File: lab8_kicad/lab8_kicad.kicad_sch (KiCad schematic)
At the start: 24 parts, among them M1 Motor, SW1 Reset, U1 SN754410, U2 PIC32MX170F256B, U4 Quadrature_Encoder

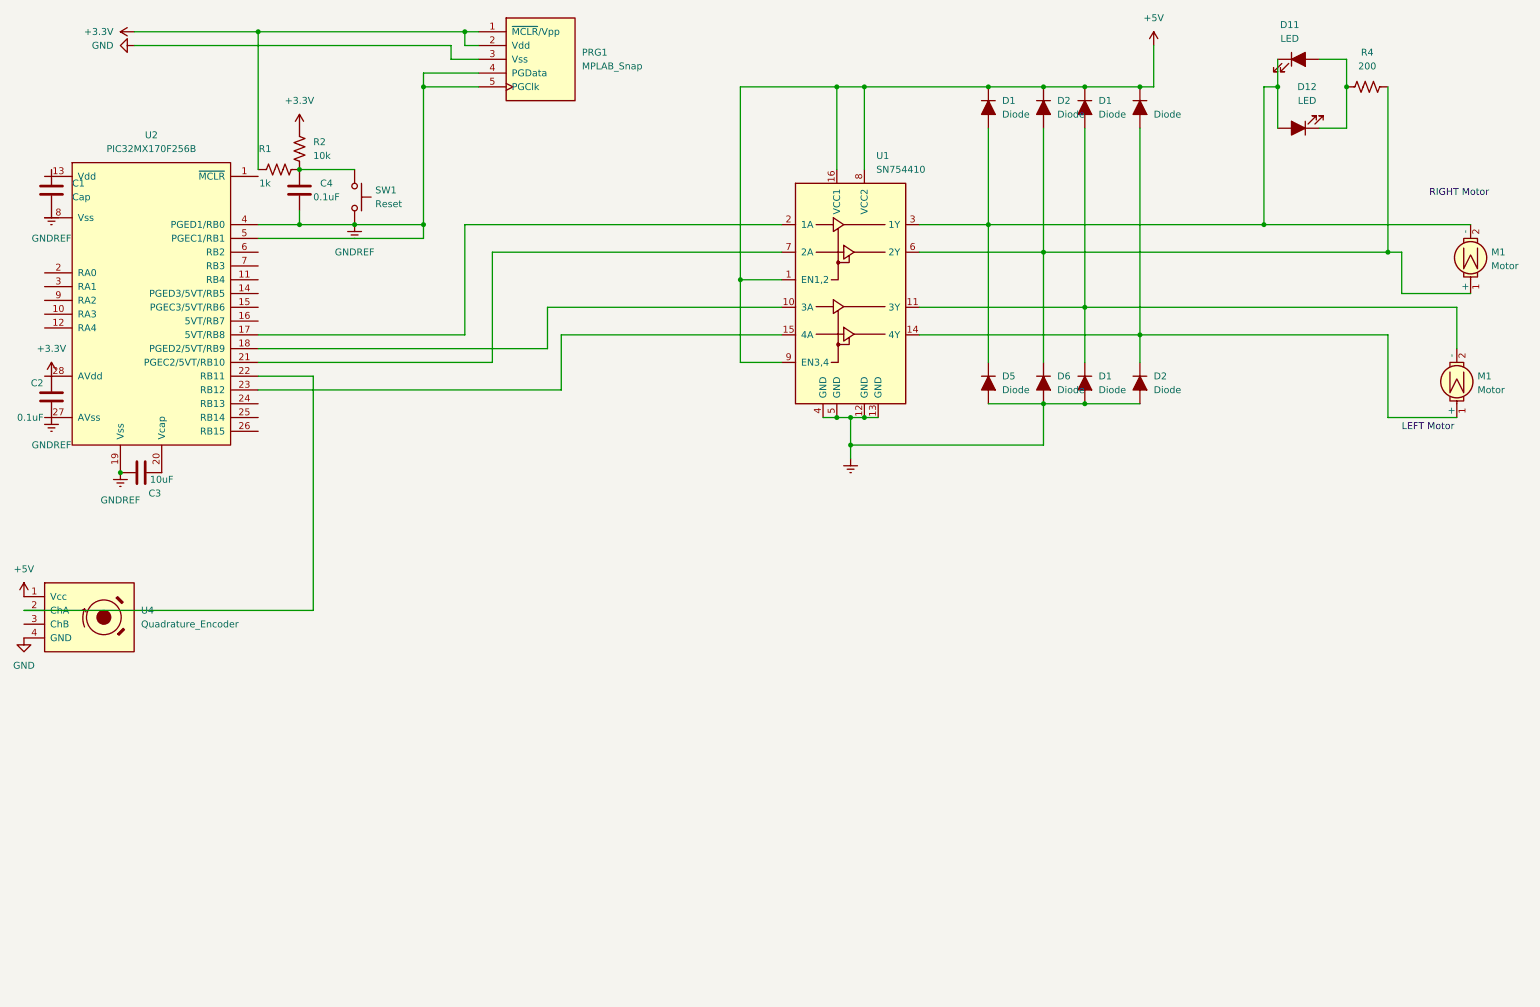
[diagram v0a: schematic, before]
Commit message: Updated Circuit Schematic (Include Cmd Gen)
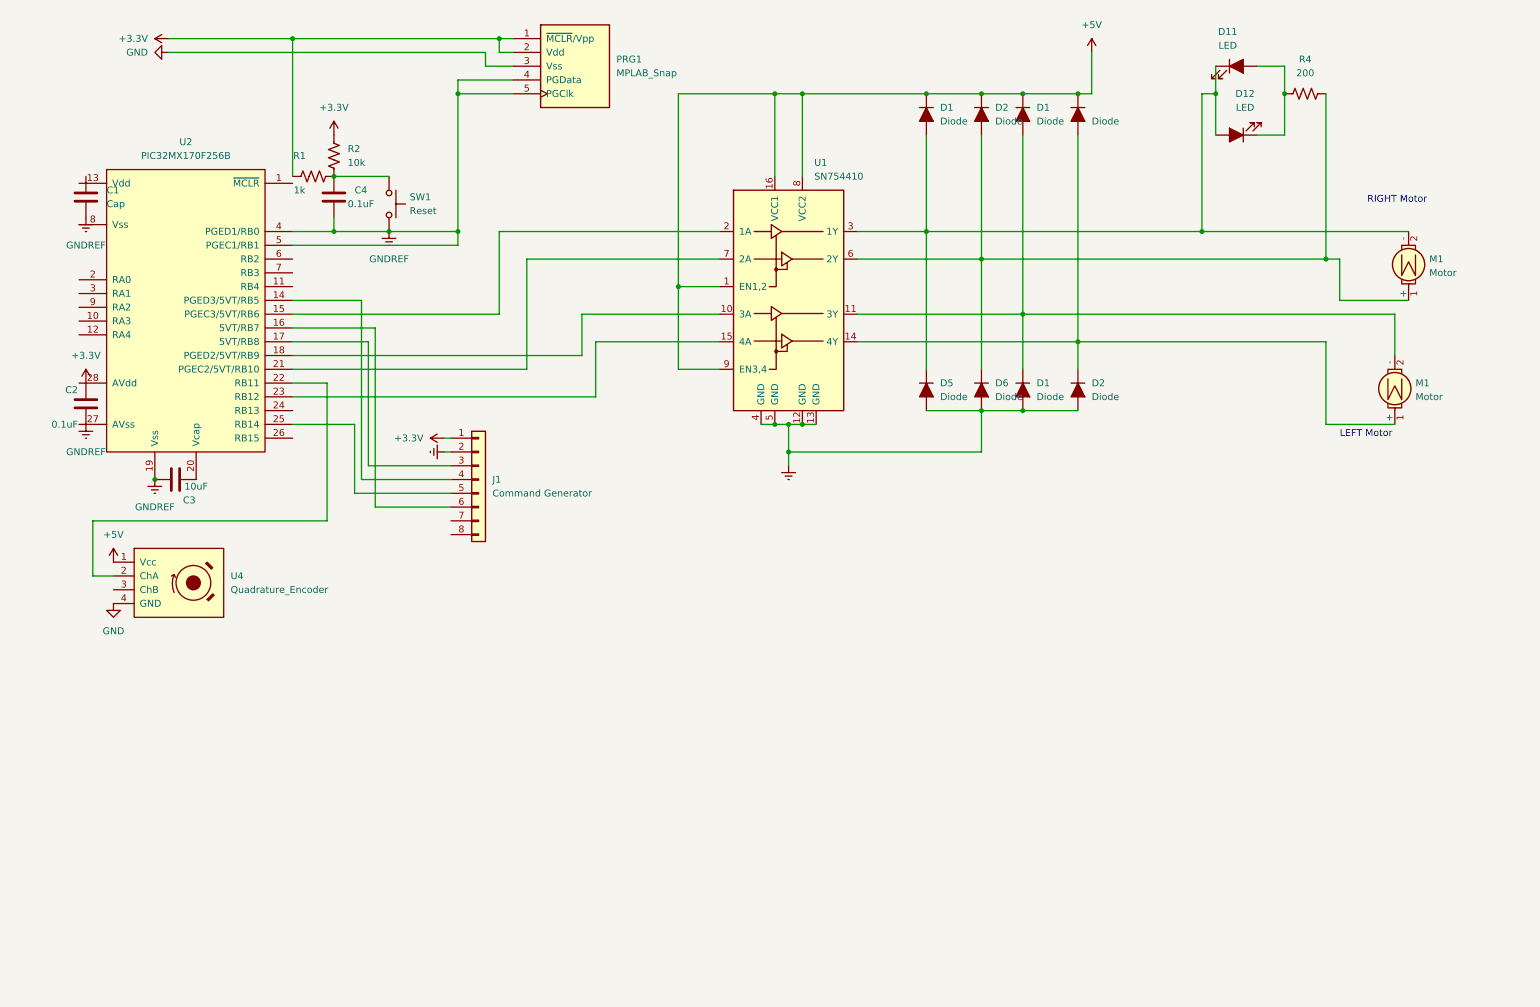
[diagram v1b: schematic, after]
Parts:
- added J1: Command Generator, symbol ME218_BaseLib:Molex8
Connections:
- net +3.3V: now also J1.1 (Pin_1)
- net Earth: now also J1.2 (Pin_2)
- net at U2.17 (5VT/RB8): now also J1.3 (Pin_3); no longer U1.2 (1A)
- net at U2.14 (PGED3/5VT/RB5): now also J1.4 (Pin_4)
- net at U2.15 (PGEC3/5VT/RB6): now also U1.2 (1A)
- net at U2.16 (5VT/RB7): now also J1.6 (Pin_6)
- net at U2.25 (RB14): now also J1.5 (Pin_5)
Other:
- moved on the sheet: C1, C2, C3, C4, D1, D11, D12, D2, D5, D6, M1, PRG1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

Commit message: fix schematic
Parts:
- removed U4: Quadrature_Encoder, symbol ME218_BaseLib:Quadrature_Encoder
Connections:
- net +3.3V: no longer PRG1.1 (~{MCLR}/Vpp), R1.1
- net GNDREF: no longer PRG1.4 (PGData), PRG1.5 (PGClk), U2.4 (PGED1/RB0), U2.5 (PGEC1/RB1)
- net at J1.6 (Pin_6): now also U2.11 (RB4); no longer U2.16 (5VT/RB7)
- net at U2.1 (~{MCLR}): now also PRG1.1 (~{MCLR}/Vpp), R1.1
- new net: PRG1.4 (PGData), U2.4 (PGED1/RB0)
- new net: PRG1.5 (PGClk), U2.5 (PGEC1/RB1)
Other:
- moved on the sheet: C1, C2, C3, C4, D1, D11, D12, D2, D5, D6, J1, M1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

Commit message: suibian
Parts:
- added J2: Reflective Opto-sensor, symbol ME218_BaseLib:Molex4
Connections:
- net +3.3V: now also J2.1 (Pin_1)
- net GND: now also J2.2 (Pin_2)
- net BI-CONSENSOR: now reaches U2.23 (RB12)
- net BI-CONSENSOR: no longer U1.15 (4A)
- net at U1.2 (1A): now also U2.6 (RB2); no longer U2.15 (PGEC3/5VT/RB6)
- net OC1: now reaches U1.7 (2A)
- net OC1: now also U2.7 (RB3); no longer U2.21 (PGEC2/5VT/RB10)
- net tera: now reaches U2.16 (5VT/RB7)
- net tera: now also U2.15 (PGEC3/5VT/RB6)
- net tape sensor: now reaches U2.9 (RA2)
- net tape sensor: now also J2.3 (Pin_3)
- new net OC3: U1.15 (4A), U2.21 (PGEC2/5VT/RB10)
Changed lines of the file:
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@@
+    (stroke (width 0) (type default))
+  )
+  (wire (pts (xy 104.14 60.96) (xy 66.04 60.96))
+    (stroke (width 0) (type default))
+  )
+  (wire (pts (xy 104.14 55.88) (xy 104.14 60.96))
     (stroke (width 0) (type default))
   )
@@
     (stroke (width 0) (type default))
   )
-  (wire (pts (xy 104.14 55.88) (xy 104.14 71.12))
-    (stroke (width 0) (type default))
-  )
   (wire (pts (xy 210.82 38.1) (xy 210.82 76.2))
     (stroke (width 0) (type default))
@@
     (stroke (width 0) (type default))
   )
+  (wire (pts (xy 109.22 63.5) (xy 66.04 63.5))
+    (stroke (width 0) (type default))
+  )
   (wire (pts (xy 256.54 91.44) (xy 269.24 91.44))
     (stroke (width 0) (type default))
   )
-  (wire (pts (xy 109.22 60.96) (xy 109.22 81.28))
-    (stroke (width 0) (type default))
-  )
   (wire (pts (xy 259.08 68.58) (xy 271.78 68.58))
     (stroke (width 0) (type default))
   )
-  (wire (pts (xy 66.04 71.12) (xy 104.14 71.12))
-    (stroke (width 0) (type default))
-  )
   (wire (pts (xy 73.66 38.1) (xy 83.82 38.1))
     (stroke (width 0) (type default))
@@
     (stroke (width 0) (type default))
   )
-  (wire (pts (xy 121.92 86.36) (xy 121.92 76.2))
+  (wire (pts (xy 96.52 81.28) (xy 66.04 81.28))
+    (stroke (width 0) (type default))
+  )
+  (wire (pts (xy 20.32 128.27) (xy 20.32 69.85))
+    (stroke (width 0) (type default))
+  )
+  (wire (pts (xy 96.52 76.2) (xy 96.52 81.28))
     (stroke (width 0) (type default))
   )
@@
     (stroke (width 0) (type default))
   )
-  (wire (pts (xy 119.38 78.74) (xy 119.38 71.12))
-    (stroke (width 0) (type default))
-  )
-  (wire (pts (xy 121.92 76.2) (xy 144.78 76.2))
-    (stroke (width 0) (type default))
-  )
-  (wire (pts (xy 119.38 71.12) (xy 144.78 71.12))
+  (wire (pts (xy 91.44 78.74) (xy 66.04 78.74))
     (stroke (width 0) (type default))
   )
@@
     (stroke (width 0) (type default))
   )
+  (wire (pts (xy 20.32 69.85) (xy 26.67 69.85))
+    (stroke (width 0) (type default))
+  )
   (wire (pts (xy 144.78 66.04) (xy 137.16 66.04))
     (stroke (width 0) (type default))
@@
     (stroke (width 0) (type default))
   )
-  (wire (pts (xy 66.04 86.36) (xy 121.92 86.36))
+  (wire (pts (xy 106.68 128.27) (xy 20.32 128.27))
     (stroke (width 0) (type default))
   )
@@
     (stroke (width 0) (type default))
   )
+  (wire (pts (xy 144.78 76.2) (xy 96.52 76.2))
+    (stroke (width 0) (type default))
+  )
   (wire (pts (xy 243.84 25.4) (xy 248.92 25.4))
     (stroke (width 0) (type default))
@@
     (stroke (width 0) (type default))
   )
+  (wire (pts (xy 144.78 71.12) (xy 91.44 71.12))
+    (stroke (width 0) (type default))
+  )
   (wire (pts (xy 193.04 38.1) (xy 193.04 60.96))
     (stroke (width 0) (type default))
@@
     (stroke (width 0) (type default))
   )
-  (wire (pts (xy 66.04 81.28) (xy 109.22 81.28))
-    (stroke (width 0) (type default))
-  )
-  (wire (pts (xy 66.04 78.74) (xy 119.38 78.74))
+  (wire (pts (xy 91.44 71.12) (xy 91.44 78.74))
+    (stroke (width 0) (type default))
+  )
+  (wire (pts (xy 109.22 60.96) (xy 109.22 63.5))
     (stroke (width 0) (type default))
   )
@@
   (text "RIGHT Motor" (at 262.89 49.53 0)
     (effects (font (size 1.27 1.27)) (justify left bottom))
+  )
+  (global_label "tera" (shape input) (at 66.04 71.12 0) (fields_autoplaced)
+    (effects (font (size 1.27 1.27)) (justify left))
+    (property "Intersheetrefs" "${INTERSHEET_REFS}" (at 72.7747 71.12 0)
+      (effects (font (size 1.27 1.27)) (justify left) hide)
+    )
+  )
+  (global_label "OC3" (shape input) (at 102.87 76.2 0) (fields_autoplaced)
+    (effects (font (size 1.27 1.27)) (justify left))
+    (property "Intersheetrefs" "${INTERSHEET_REFS}" (at 109.6652 76.2 0)
+      (effects (font (size 1.27 1.27)) (justify left) hide)
+    )
+  )
+  (global_label "tape sensor" (shape input) (at 66.04 128.27 180) (fields_autoplaced)
+    (effects (font (size 1.27 1.27)) (justify right))
+    (property "Intersheetrefs" "${INTERSHEET_REFS}" (at 51.7459 128.27 0)
+      (effects (font (size 1.27 1.27)) (justify right) hide)
+    )
+  )
+  (global_label "BI-CONSENSOR" (shape input) (at 66.04 86.36 0) (fields_autoplaced)
+    (effects (font (size 1.27 1.27)) (justify left))
+    (property "Intersheetrefs" "${INTERSHEET_REFS}" (at 83.9024 86.36 0)
+      (effects (font (size 1.27 1.27)) (justify left) hide)
+    )
+  )
+  (global_label "tera" (shape input) (at 66.04 73.66 0) (fields_autoplaced)
+    (effects (font (size 1.27 1.27)) (justify left))
+    (property "Intersheetrefs" "${INTERSHEET_REFS}" (at 72.7747 73.66 0)
+      (effects (font (size 1.27 1.27)) (justify left) hide)
+    )
+  )
+  (global_label "OC1" (shape input) (at 101.6 63.5 0) (fields_autoplaced)
+    (effects (font (size 1.27 1.27)) (justify left))
+    (property "Intersheetrefs" "${INTERSHEET_REFS}" (at 108.3952 63.5 0)
+      (effects (font (size 1.27 1.27)) (justify left) hide)
+    )
   )
   (symbol (lib_id "ME218_BaseLib:SW_Push") (at 83.82 43.18 270) (unit 1)
@@
         (path "/c54286ed-3a82-4325-b913-88d6215d969b"
           (reference "D1") (unit 1)
+        )
+      )
+    )
+  )
+  (symbol (lib_id "power:+3.3V") (at 106.68 123.19 90) (unit 1)
+    (in_bom yes) (on_board yes) (dnp no) (fields_autoplaced)
+    (property "Reference" "#PWR09" (at 110.49 123.19 0)
+      (effects (font (size 1.27 1.27)) hide)
+    )
+    (property "Value" "+3.3V" (at 102.87 123.19 90)
+      (effects (font (size 1.27 1.27)) (justify left))
+    )
+    (property "Footprint" "" (at 106.68 123.19 0)
+      (effects (font (size 1.27 1.27)) hide)
+    )
+    (property "Datasheet" "" (at 106.68 123.19 0)
+      (effects (font (size 1.27 1.27)) hide)
+    )
+    (pin "1")
+    (instances
+      (project "lab8_kicad"
+        (path "/c3d935fb-33dd-45da-8182-93745821b586"
+          (reference "#PWR09") (unit 1)
         )
       )
@@
     )
   )
+  (symbol (lib_id "ME218_BaseLib:Molex4") (at 111.76 125.73 0) (unit 1)
+    (in_bom yes) (on_board yes) (dnp no) (fields_autoplaced)
+    (property "Reference" "J2" (at 114.3 125.73 0)
+      (effects (font (size 1.27 1.27)) (justify left))
+    )
+    (property "Value" "Reflective Opto-sensor" (at 114.3 128.27 0)
+      (effects (font (size 1.27 1.27)) (justify left))
+    )
+    (property "Footprint" "" (at 111.76 125.73 0)
+      (effects (font (size 1.27 1.27)) hide)
+    )
+    (property "Datasheet" "" (at 111.76 125.73 0)
+      (effects (font (size 1.27 1.27)) hide)
+    )
+    (pin "1")
+    (pin "2")
+    (pin "3")
+    (pin "4")
+    (instances
+      (project "lab8_kicad"
+        (path "/c3d935fb-33dd-45da-8182-93745821b586"
+          (reference "J2") (unit 1)
+        )
+      )
+    )
+  )
   (symbol (lib_id "ME218_BaseLib:LED") (at 240.03 25.4 0) (unit 1)
     (in_bom yes) (on_board yes) (dnp no) (fields_autoplaced)
@@
         )
       )
+    )
+  )
+  (symbol (lib_id "power:GND") (at 106.68 125.73 270) (unit 1)
+    (in_bom yes) (on_board yes) (dnp no) (fields_autoplaced)
+    (property "Reference" "#PWR010" (at 100.33 125.73 0)
+      (effects (font (size 1.27 1.27)) hide)
+    )
+    (property "Value" "GND" (at 102.87 125.73 90)
+      (effects (font (size 1.27 1.27)) (justify right))
+    )
+    (property "Footprint" "" (at 106.68 125.73 0)
+      (effects (font (size 1.27 1.27)) hide)
+    )
+    (property "Datasheet" "" (at 106.68 125.73 0)
+      (effects (font (size 1.27 1.27)) hide)
+    )
+    (pin "1")
+    (instances
+      (project "lab8_kicad"
+        (path "/c3d935fb-33dd-45da-8182-93745821b586"
+          (reference "#PWR010") (unit 1)
+        )
+      )

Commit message: fix schemetic
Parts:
- removed D11, D12: LED, symbol ME218_BaseLib:LED
- added Q1: Photo_NPN, symbol ME218_BaseLib:Photo_NPN
- added R5, R6: 10K, symbol ME218_BaseLib:Res1
- added U2: MCP6294, symbol ME218_BaseLib:MCP6294
- R4: value 200 -> 2K
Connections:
- net +5V: now also Q1.1 (C), R5.1, U2.4 (V+)
- net Earth: now also R6.2, U2.11 (V-)
- net at R4.1: now also Q1.2 (E), U2.2 (-)
- net at D2.2 (A), D6.1 (K), M1.1 (+)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: no longer R4.2
- net BI-CONSENSOR renamed BEACON_SENSOR
- net BEACON_SENSOR: now also R4.2, U2.1
- new net: R5.2, R6.1, U2.3 (+)

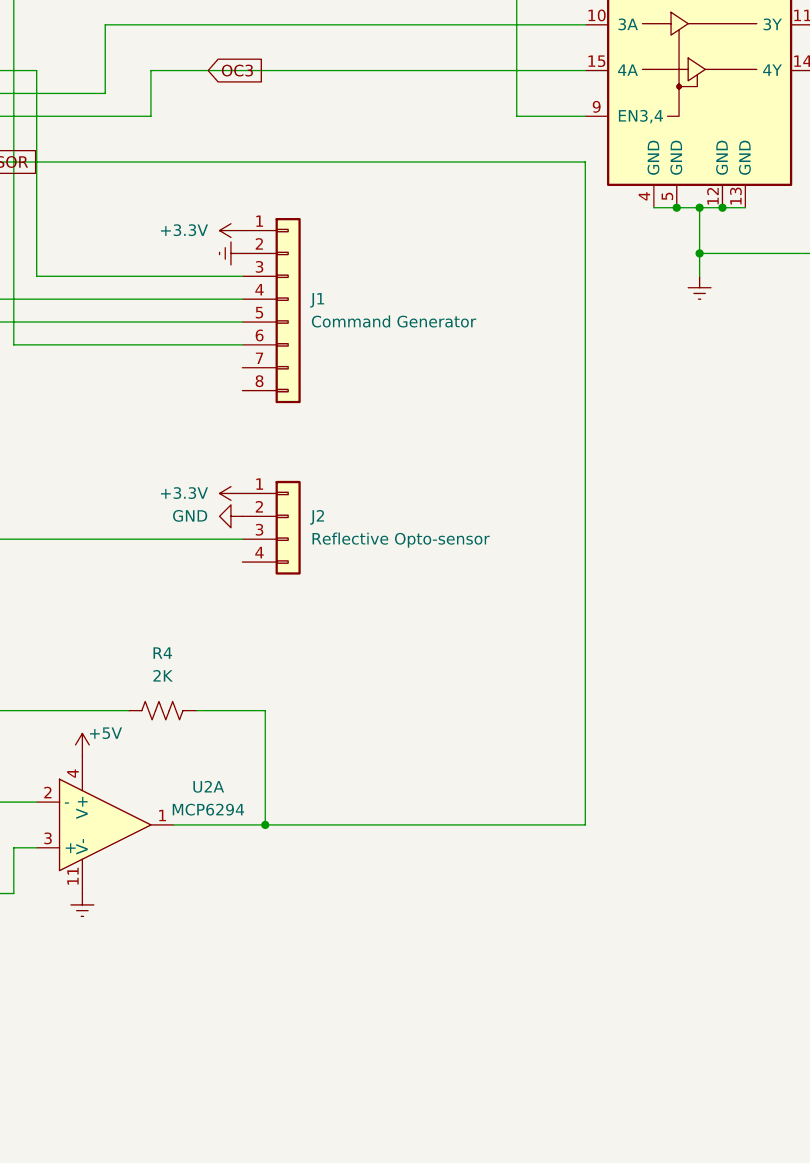
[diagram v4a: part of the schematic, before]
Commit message: add comparator
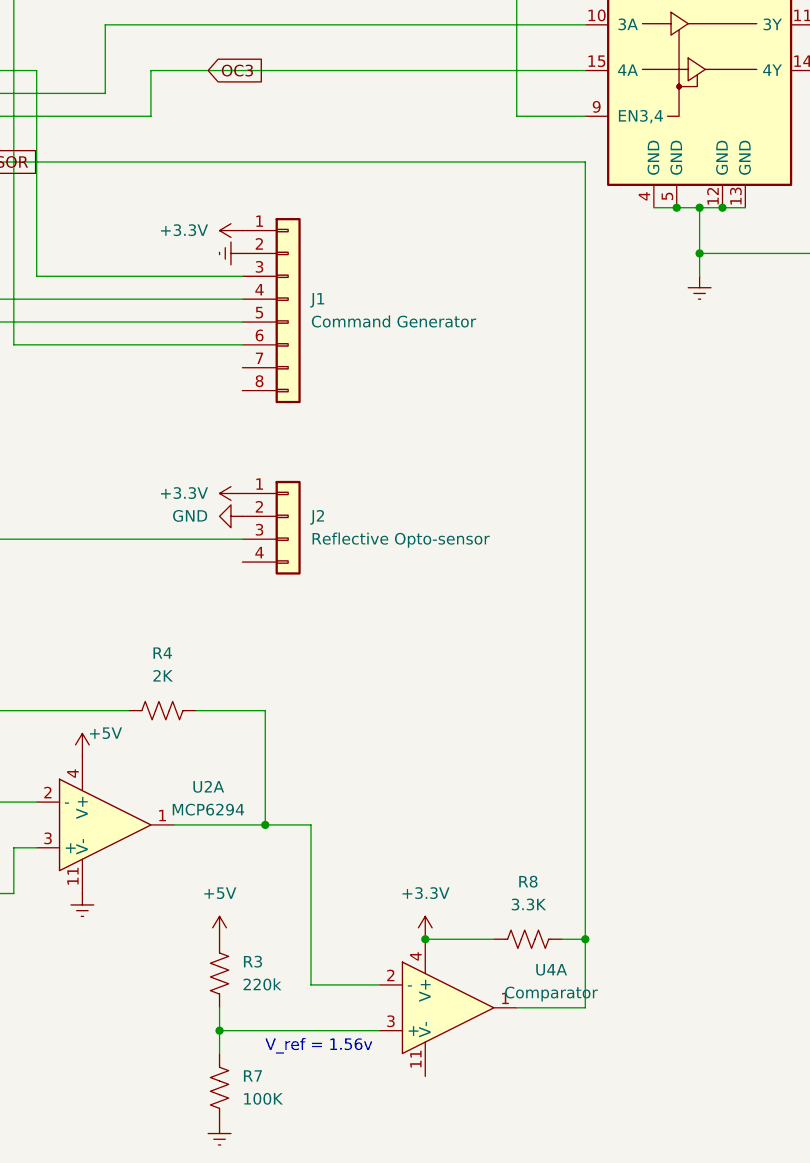
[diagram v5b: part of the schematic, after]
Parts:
- added R3: 220k, symbol ME218_BaseLib:Res1
- added R7: 100K, symbol ME218_BaseLib:Res1
- added R8: 3.3K, symbol ME218_BaseLib:Res1
- added U4: Comparator, symbol ME218_BaseLib:MCP6294
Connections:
- net +3.3V: now also R8.1, U4.4 (V+)
- net +5V: now also R3.1
- net BEACON_SENSOR: now also R8.2, U4.1; no longer R4.2, U2.1
- net Earth: now also R7.2
- new net: R4.2, U2.1, U4.2 (-)
- new net: R3.2, R7.1, U4.3 (+)
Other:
- note added: "V_ref = 1.56v"
